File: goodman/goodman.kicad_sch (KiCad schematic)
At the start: 1 part, among them J1 TSM-110-01-T-DV

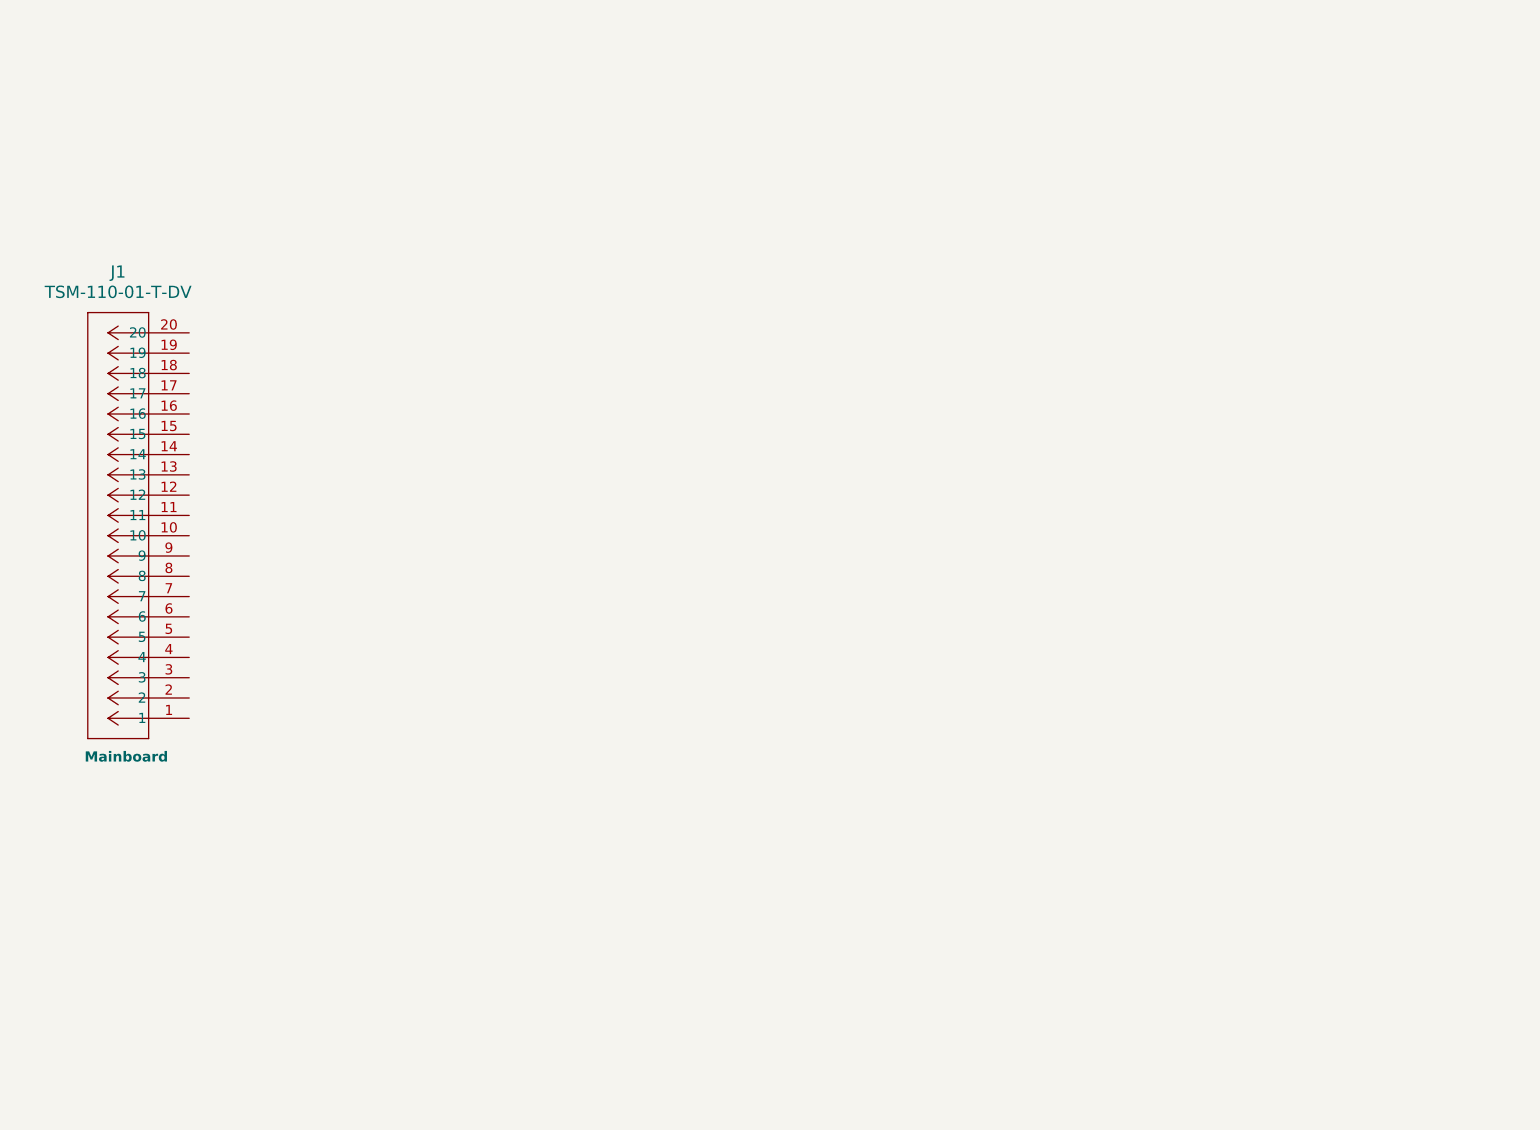
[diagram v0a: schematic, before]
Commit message: Added some wire connections and filter logic.
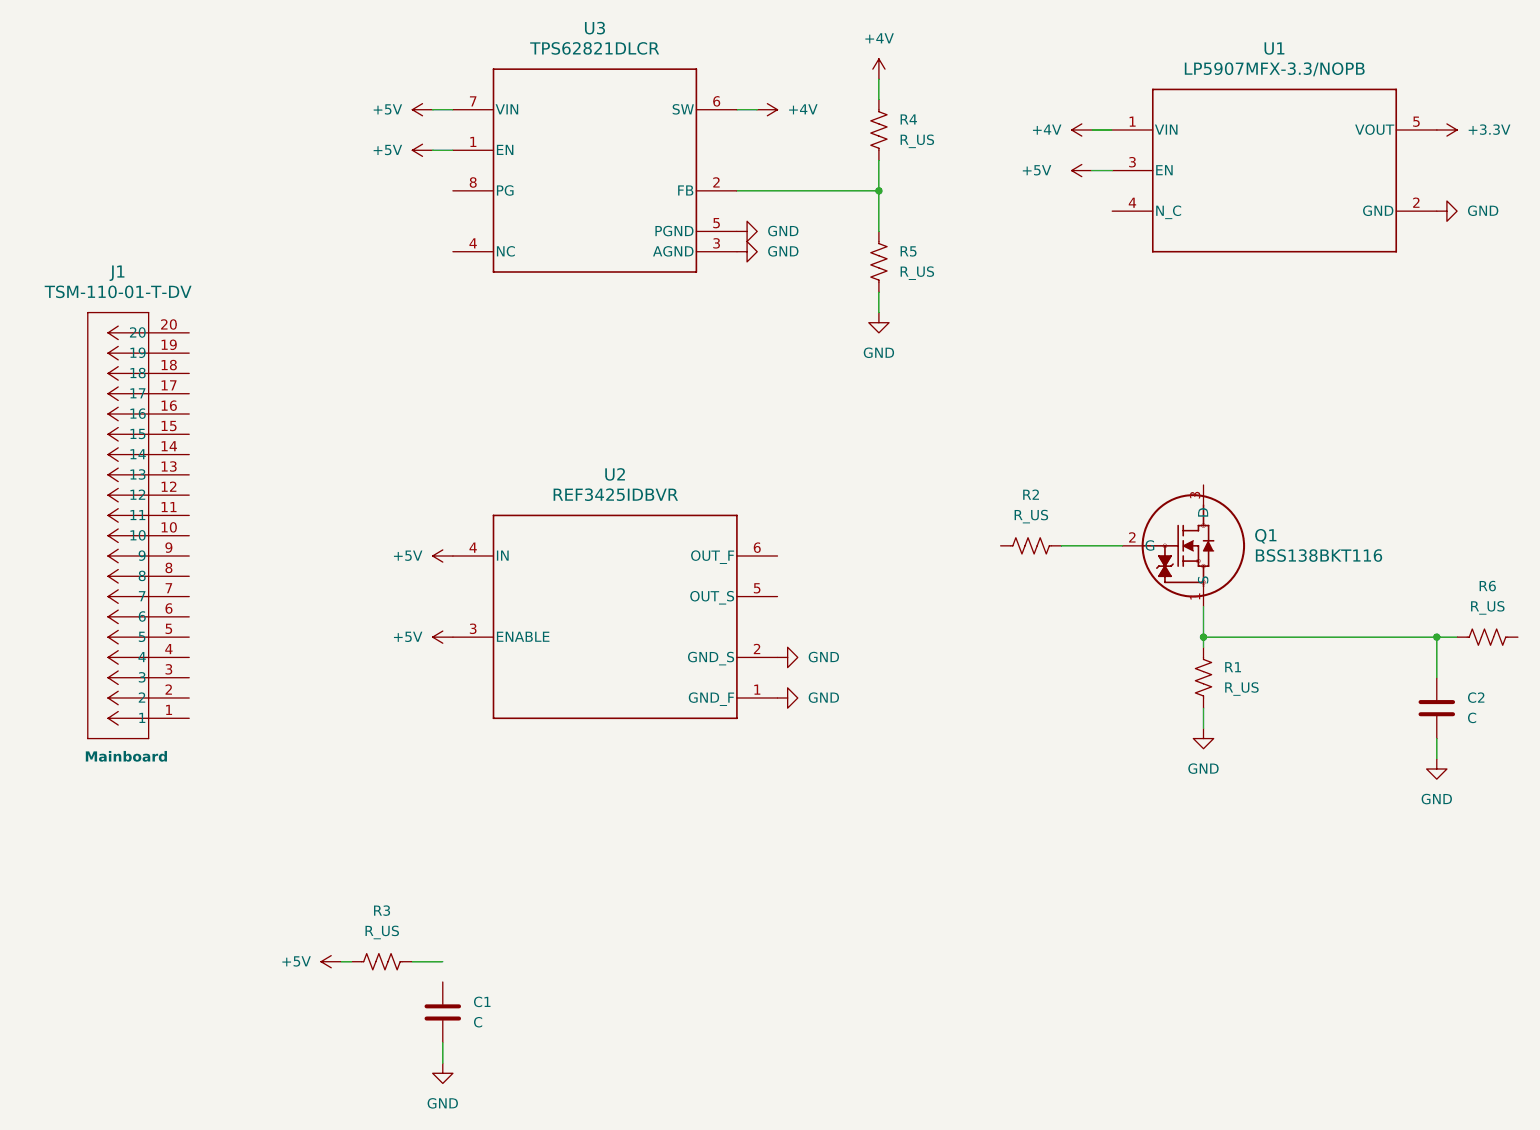
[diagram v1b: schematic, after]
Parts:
- added C1, C2: C, symbol Device:C
- added Q1: BSS138BKT116, SOT23_BSS138_ROM, symbol Goodman Local:BSS138BKT116
- added R1, R2, R3, R4, R5, R6: R_US, symbol Device:R_US
- added U1: LP5907MFX-3.3/NOPB, DBV0005A_N, symbol Goodman Local:LP5907MFX-3.3_NOPB
- added U2: REF3425IDBVR, DBV0006A_N, symbol Goodman Local:REF3425IDBVR
- added U3: TPS62821DLCR, DLC0008A, symbol Goodman Local:TPS62821DLCR
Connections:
- new net: C2.1, Q1.1 (S), R1.1, R6.1
- new net: R4.2, R5.1, U3.2 (FB)
- new net: Q1.2 (G), R2.2
- new net +3.3V: U1.5 (VOUT)
- new net +4V: R4.1, U1.1 (VIN), U3.6 (SW)
- new net +5V: R3.1, U1.3 (EN), U2.3 (ENABLE), U2.4 (IN), U3.1 (EN), U3.7 (VIN)
- new net GND: C1.2, C2.2, R1.2, R5.2, U1.2 (GND), U2.1 (GND_F), U2.2 (GND_S), U3.3 (AGND), U3.5 (PGND)
